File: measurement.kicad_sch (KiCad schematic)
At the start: 16 parts, among them U26001 ACS730xLCTR-20AB, U26002 TLV9352

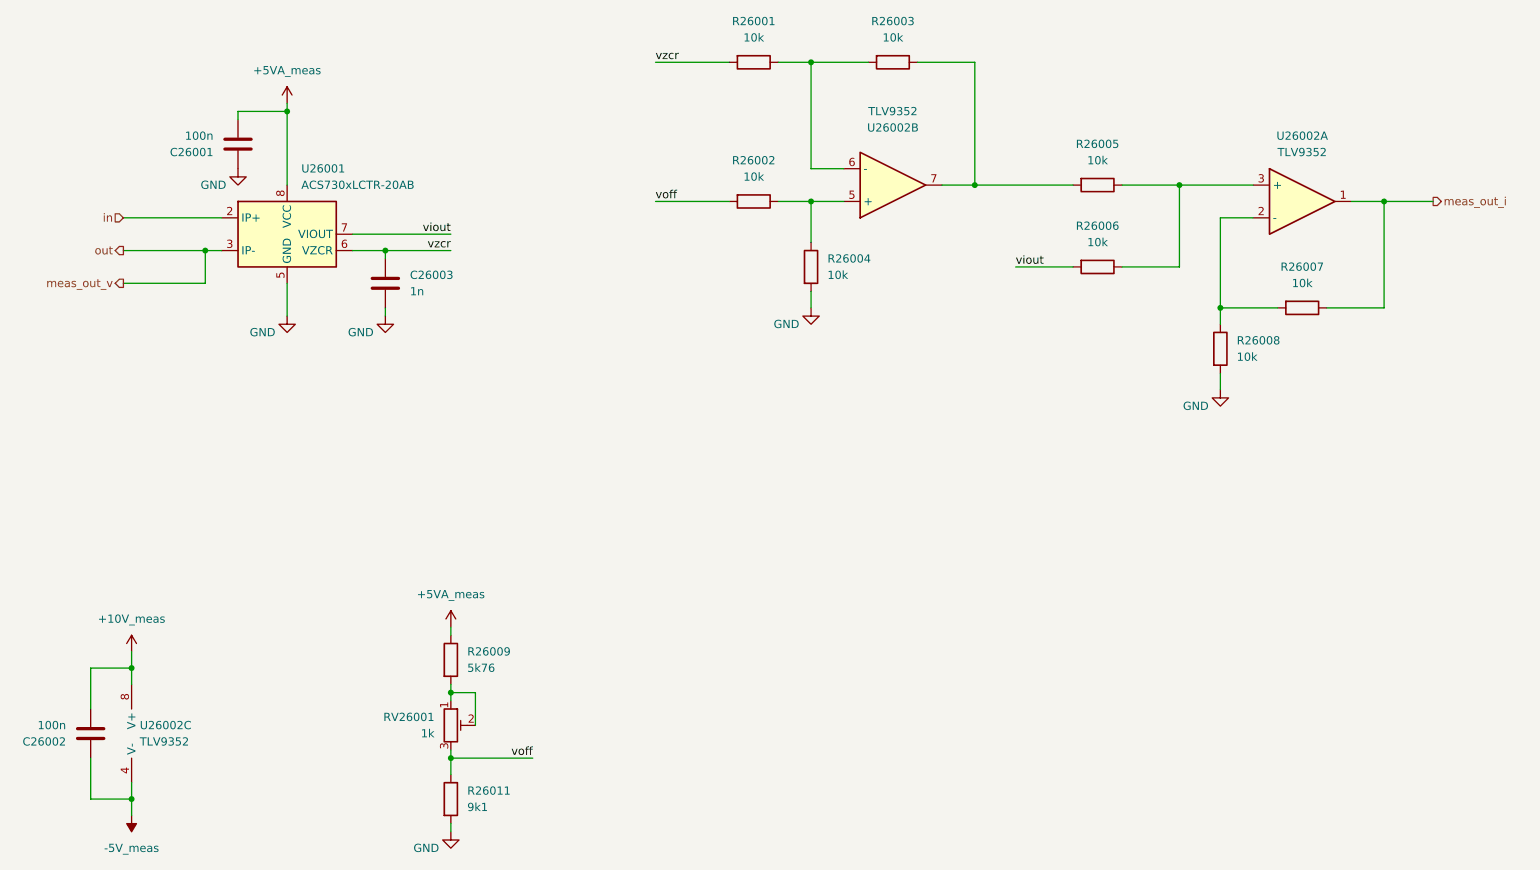
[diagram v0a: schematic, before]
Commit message: add pss 3dmodels and testpoints
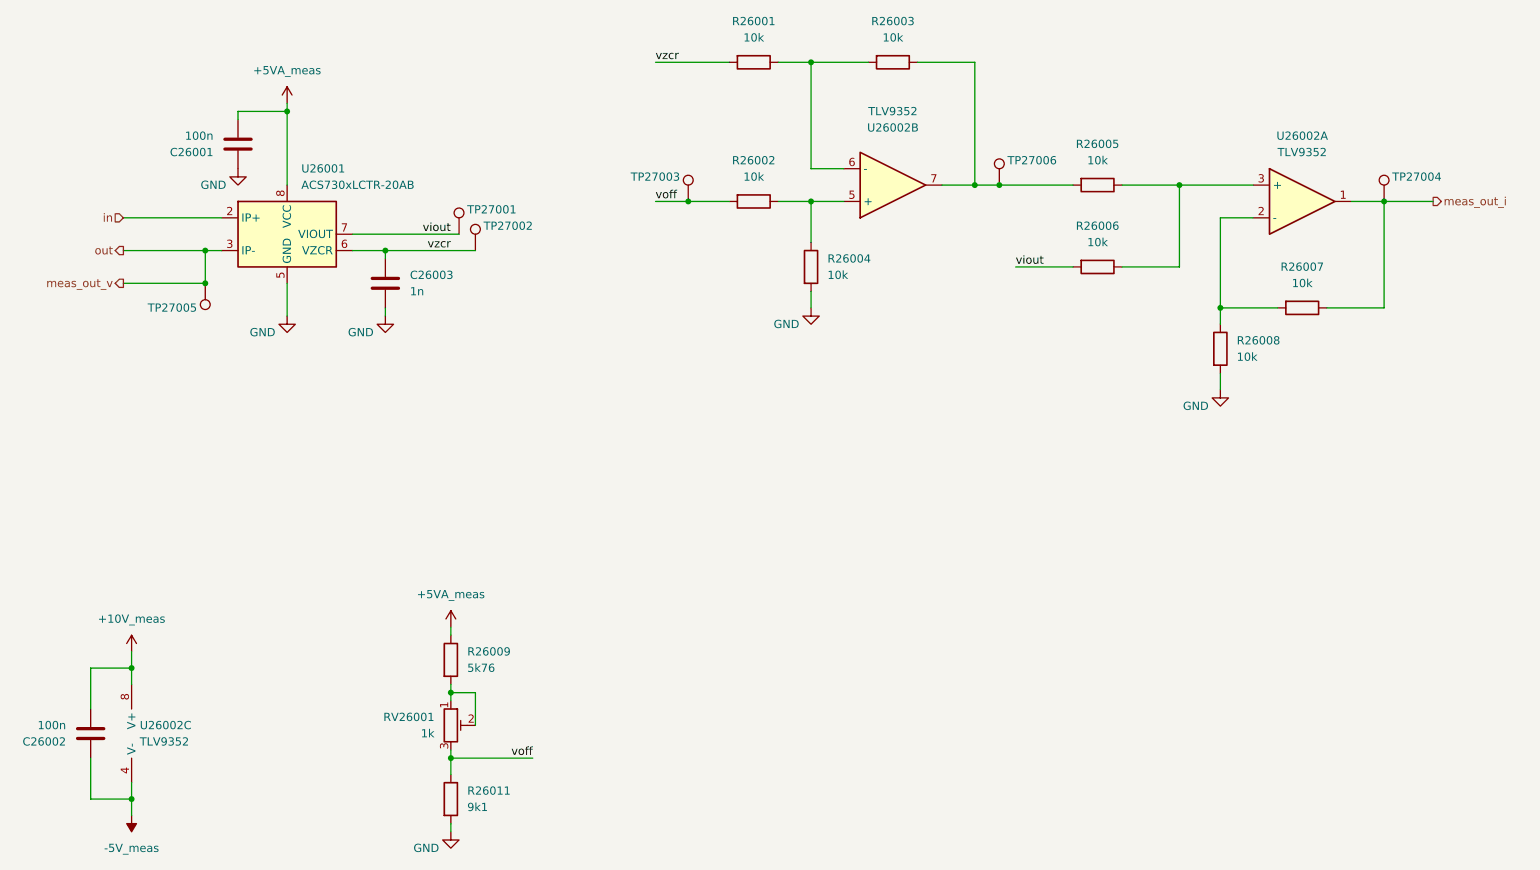
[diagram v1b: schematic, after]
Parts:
- added TP27001, TP27002, TP27003, TP27004, TP27005, TP27006: ~, pss:TP_0805_2012Metric, symbol Connector:TestPoint
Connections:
- net meas_out_i: now also TP27004.1
- net meas_out_v: now also TP27005.1
- net viout: now also TP27001.1
- net voff: now also TP27003.1
- net vzcr: now also TP27002.1
- net at R26003.1, R26005.2, U26002.7: now also TP27006.1

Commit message: edit pss symbol library: export all schematic symbols to library 'pss' and update symbol link
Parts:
- RV26001: symbol Device:R_Potentiometer_Trim -> pss:R_Potentiometer_Trim
- TP27001, TP27002, TP27003, TP27004, TP27005, TP27006: symbol Connector:TestPoint -> pss:TestPoint
- U26001: symbol Sensor_Current:ACS730xLCTR-20AB -> pss:ACS730xLCTR-20AB
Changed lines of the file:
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@@
 	)
 	(symbol
-		(lib_id "Connector:TestPoint")
+		(lib_id "pss:TestPoint")
 		(at 105.41 95.25 0)
 		(unit 1)
@@
 	)
 	(symbol
-		(lib_id "Connector:TestPoint")
+		(lib_id "pss:TestPoint")
 		(at 246.38 87.63 0)
 		(unit 1)
@@
 	)
 	(symbol
-		(lib_id "Connector:TestPoint")
+		(lib_id "pss:TestPoint")
 		(at 186.69 85.09 0)
 		(unit 1)
@@
 	)
 	(symbol
-		(lib_id "Sensor_Current:ACS730xLCTR-20AB")
+		(lib_id "pss:ACS730xLCTR-20AB")
 		(at 76.2 92.71 0)
 		(unit 1)
@@
 	)
 	(symbol
-		(lib_id "Connector:TestPoint")
+		(lib_id "pss:TestPoint")
 		(at 138.43 87.63 0)
 		(mirror y)
@@
 	)
 	(symbol
-		(lib_id "Connector:TestPoint")
+		(lib_id "pss:TestPoint")
 		(at 63.5 100.33 180)
 		(unit 1)
@@
 	)
 	(symbol
-		(lib_id "Device:R_Potentiometer_Trim")
+		(lib_id "pss:R_Potentiometer_Trim")
 		(at 101.6 168.91 0)
 		(unit 1)
@@
 	)
 	(symbol
-		(lib_id "Connector:TestPoint")
+		(lib_id "pss:TestPoint")
 		(at 102.87 92.71 0)
 		(unit 1)
